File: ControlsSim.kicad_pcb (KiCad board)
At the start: 2 copper layers, 100 x 100 mm, 26 parts, among them J2 Accelerator Pot, J3 Brake Button, J5 Motor Contactors, J6 Array Contactors, J7 Rotary Switch, SW2 SW_Rotary2x6

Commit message: Updated silkscreen that Controls wanted
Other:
- board text added: "IGN_1"
- board text added: "IGN_2"
- board text added: "LOW_V"
- board text added: "MAX"
- board text added: "MIN"
- board text added: "OFF"
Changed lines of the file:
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@@
     (effects (font (size 2 2) (thickness 0.15)) (justify mirror))
+  )
+  (gr_text "IGN_2" (at 154.432 99.822) (layer "F.SilkS")
+    (effects (font (size 1 1) (thickness 0.15)) (justify left bottom))
+  )
+  (gr_text "MAX" (at 176.022 81.788) (layer "F.SilkS")
+    (effects (font (size 1 1) (thickness 0.15)) (justify left bottom))
+  )
+  (gr_text "IGN_2" (at 164.846 111.76) (layer "F.SilkS")
+    (effects (font (size 1 1) (thickness 0.15)) (justify left bottom))
   )
   (gr_text "Array Precharge" (at 130.5 67.75) (layer "F.SilkS")
     (effects (font (size 1.5 1.5) (thickness 0.15)))
+  )
+  (gr_text "IGN_2" (at 160.528 104.14) (layer "F.SilkS")
+    (effects (font (size 1 1) (thickness 0.15)) (justify left bottom))
+  )
+  (gr_text "LOW_V" (at 160.274 125.476) (layer "F.SilkS")
+    (effects (font (size 1 1) (thickness 0.15)) (justify left bottom))
+  )
+  (gr_text "OFF" (at 152.4 130.048) (layer "F.SilkS")
+    (effects (font (size 1 1) (thickness 0.15)) (justify left bottom))
   )
   (gr_text "Contactor Indicators" (at 102.25 73.25 90) (layer "F.SilkS")
@@
     (effects (font (size 1 1) (thickness 0.15)) (justify left))
   )
+  (gr_text "IGN_1" (at 165.1 117.602) (layer "F.SilkS")
+    (effects (font (size 1 1) (thickness 0.15)) (justify left bottom))
+  )
+  (gr_text "MIN" (at 176.53 131.318) (layer "F.SilkS")
+    (effects (font (size 1 1) (thickness 0.15)) (justify left bottom))
+  )
   (dimension (type orthogonal) (layer "Cmts.User")

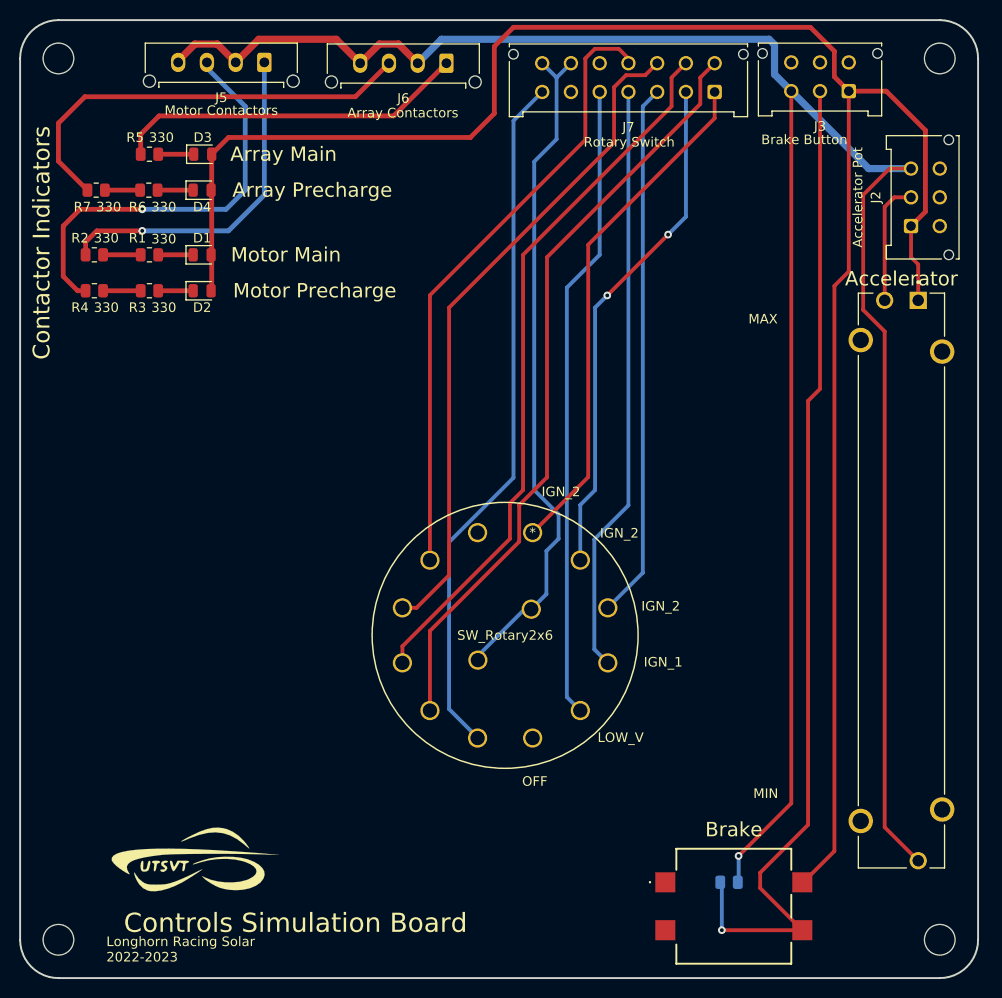
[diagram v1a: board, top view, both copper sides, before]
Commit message: Fixed resistor value and layout, fixed labels for rotary encoder.
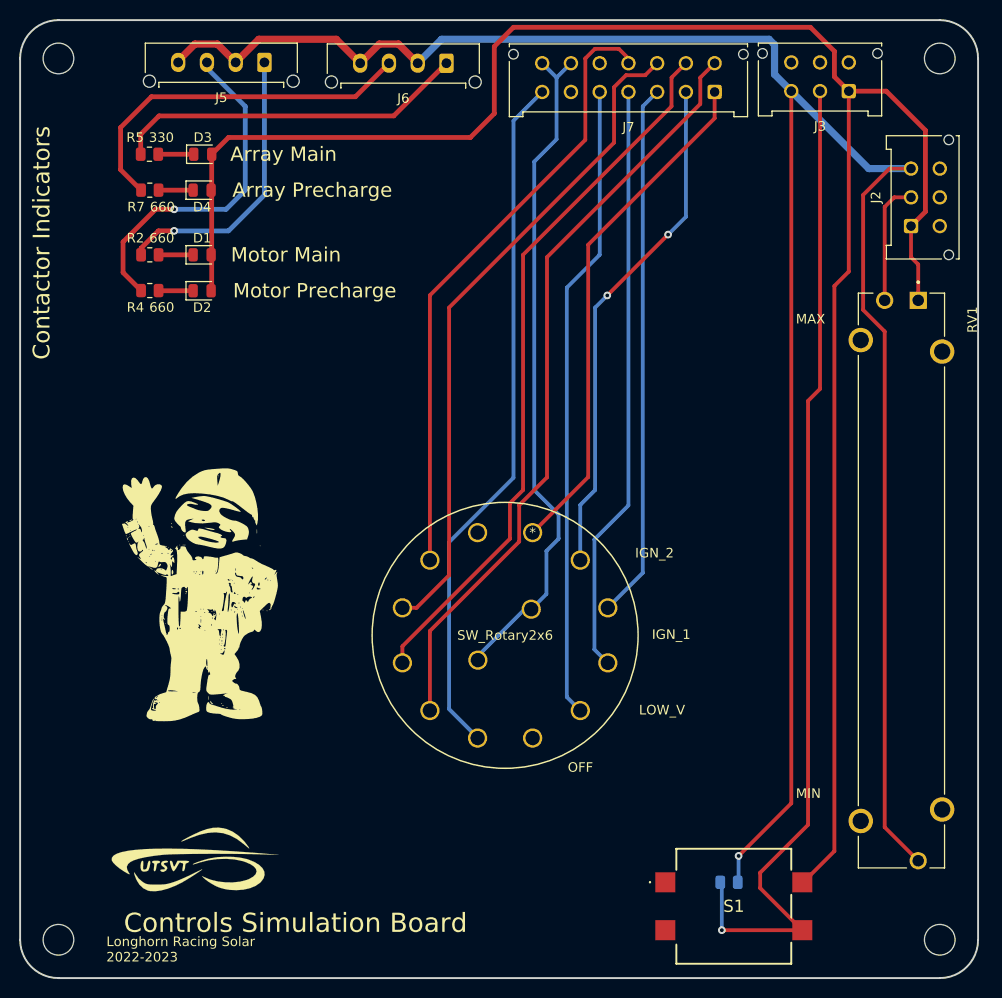
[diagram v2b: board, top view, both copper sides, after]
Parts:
- removed R1, R3, R6: 330, Resistor_SMD:R_0805_2012Metric
- added LOGO3: Babu, UTSVT_Special:Babu the Builder, F.Cu at (119.2, 109.7)
- J2, J3: footprint UTSVT_Connectors:Molex_Micro-Fit_3.0_43045-0612_2x03_P3.00mm_Vertical -> Connector_Molex:Molex_Micro-Fit_3.0_43045-0612_2x03_P3.00mm_Vertical
- J5, J6: footprint UTSVT_Connectors:Molex_Micro-Fit_3.0_43650-0415_1x04_P3.00mm_Vertical -> Connector_Molex:Molex_Micro-Fit_3.0_43650-0415_1x04_P3.00mm_Vertical
- J7: footprint UTSVT_Connectors:Molex_Micro-Fit_3.0_43045-1412_2x07_P3.00mm_Vertical -> Connector_Molex:Molex_Micro-Fit_3.0_43045-1412_2x07_P3.00mm_Vertical
- R2, R4, R7: value 330 -> 660
- RV1: footprint Footprints:PTA4543 -> UTSVT_Special:PTA4543
- S1: footprint Footprints:TS16121295BK260SMTTR -> UTSVT_Special:TS16121295BK260SMTTR
- moved R4 5.79 mm to (113.5, 78.2)
- moved R2 5.79 mm to (113.5, 74.5)
- moved R7 5.60 mm to (113.5, 67.8)
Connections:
- net /Acc_Pot_Vo renamed Acc_Pot_Vo
- net /Brk_Signal renamed Brk_Signal
- J5 pad 1: /M_D_Mn3 -> /M_D_Mn2
- J5 pad 3: /M_D_Pre3 -> /M_D_Pre2
- J6 pad 3: /A_D_Pre3 -> /A_D_Pre2
- R2 pad 1: /M_D_Mn2 -> /M_D_Mn1
- R2 pad 2: /M_D_Mn3 -> /M_D_Mn2
- R4 pad 1: /M_D_Pre3 -> /M_D_Pre2
- R4 pad 2: /M_D_Pre2 -> /M_D_Pre1
- R7 pad 1: /A_D_Pre2 -> /A_D_Pre1
- R7 pad 2: /A_D_Pre3 -> /A_D_Pre2
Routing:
- net /A_D_Pre3: track 45.3 -> 0.00 mm
- net /M_D_Pre3: track 43.8 -> 0.00 mm, vias 1 -> 0
- net /M_D_Mn3: track 35.9 -> 0.00 mm, vias 1 -> 0
- net /A_D_Pre2: track 3.68 -> 38.2 mm
- net /M_D_Pre2: track 3.93 -> 35.8 mm, vias 0 -> 1
- net /M_D_Mn2: track 3.93 -> 29.7 mm, vias 0 -> 1
